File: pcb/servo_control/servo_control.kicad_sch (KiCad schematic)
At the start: 50 parts, among them J1 USB_B_Micro, J10 Conn_01x03_Female, J11 Conn_01x03_Female, J12 Conn_01x03_Female, J13 Conn_01x03_Female, J14 Conn_01x03_Female, J15 Conn_01x03_Female, J16 Conn_01x03_Female, J17 Conn_01x03_Female, J18 Conn_01x03_Female, J19 Conn_01x03_Female, J2 YLIDAR X4, J20 Conn_01x03_Female, J21 Conn_01x06_Male, J3 Conn_01x03_Female, J4 Conn_01x03_Female, J5 Conn_01x03_Female, J6 Conn_01x03_Female, J7 Conn_01x03_Female, J8 Conn_01x03_Female, J9 Conn_01x03_Female, SW1 ESP_PROG, SW2 ESP_RST, U1 PCA9685BS, U2 LM317_SOT-223, U3 ESP32-WROOM-32, U4 MPU-9250, U5 PCA9685BS

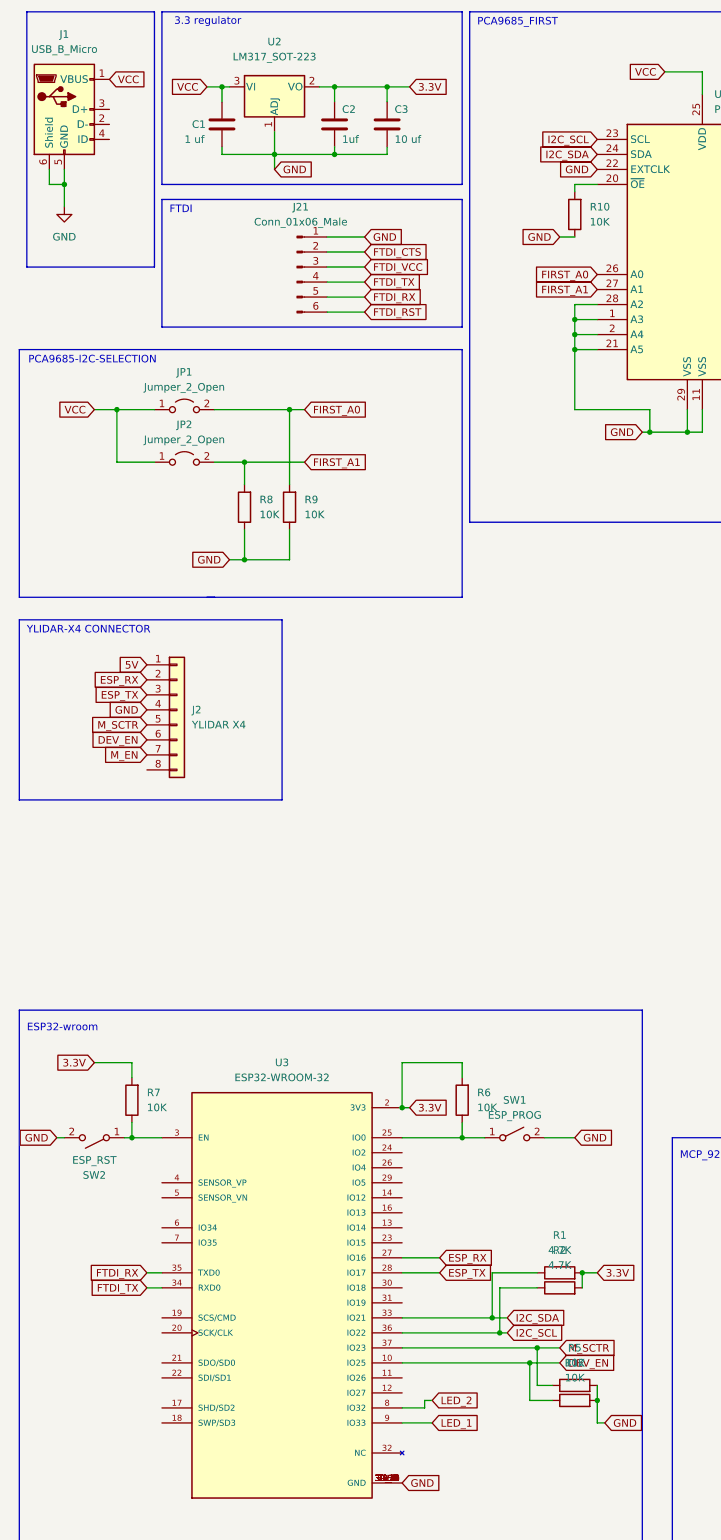
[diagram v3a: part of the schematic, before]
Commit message: add 5V regulator
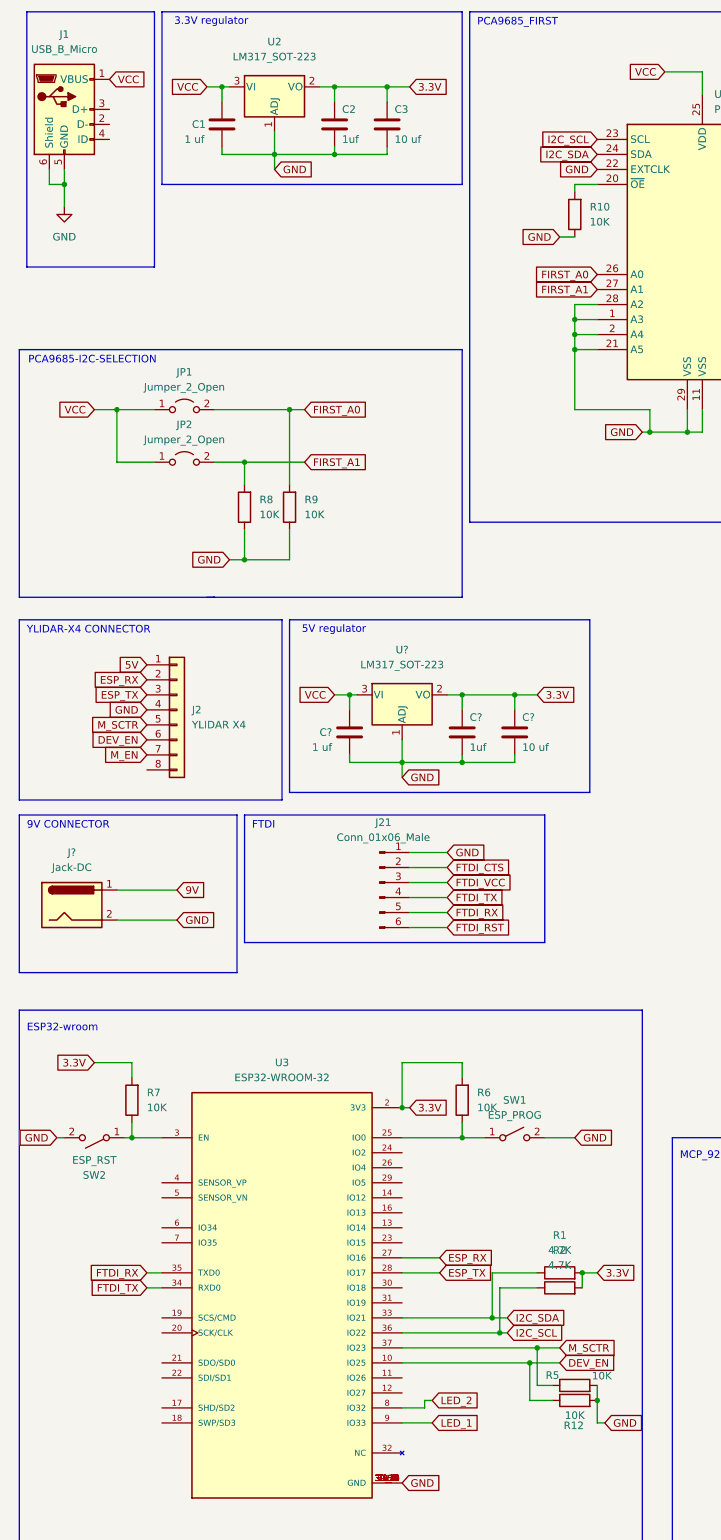
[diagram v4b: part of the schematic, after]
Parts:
- added C?: 1 uf, Capacitor_SMD:C_0603_1608Metric, symbol Device:C
- added C?: 1uf, Capacitor_SMD:C_0603_1608Metric, symbol Device:C
- added C?: 10 uf, Capacitor_SMD:C_0603_1608Metric, symbol Device:C
- added J?: Jack-DC, symbol Connector:Jack-DC
- added U?: LM317_SOT-223, Package_TO_SOT_SMD:SOT-223-3_TabPin2, symbol Regulator_Linear:LM317_SOT-223
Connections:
- net 3.3V: now also C?.1, C?.1, U?.2 (VO)
- net GND: now also C?.2, C?.2, C?.2, J?.2, U?.1 (ADJ)
- net VCC: now also C?.1, U?.3 (VI)
- new net 9V: J?.1
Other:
- note added: "3.3V regulator"
- note added: "5V regulator"
- note added: "9V CONNECTOR"
- note removed: "3.3 regulator"
- moved on the sheet: J21

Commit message: add jack
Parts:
- removed J1: USB_B_Micro, Connector_USB:USB_Micro-B_Molex-105017-0001, symbol Connector:USB_B_Micro
- J1: renamed from J?; footprint (none) -> Connector_BarrelJack:BarrelJack_Horizontal
- gave numbers to parts that had none: 4
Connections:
- net 3.3V: no longer C8.1, C9.1, U6.2 (VO)
- net 5V: now also C8.1, C9.1, U1.25 (VDD), U5.25 (VDD), U6.2 (VO)
- net 9V: now also C1.1, C7.1, U2.3 (VI), U6.3 (VI)
- net VCC: no longer C1.1, C7.1, U1.25 (VDD), U2.3 (VI), U5.25 (VDD), U6.3 (VI)
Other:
- moved on the sheet: D1, D2, R10, R11, R3, R4, U1, U5

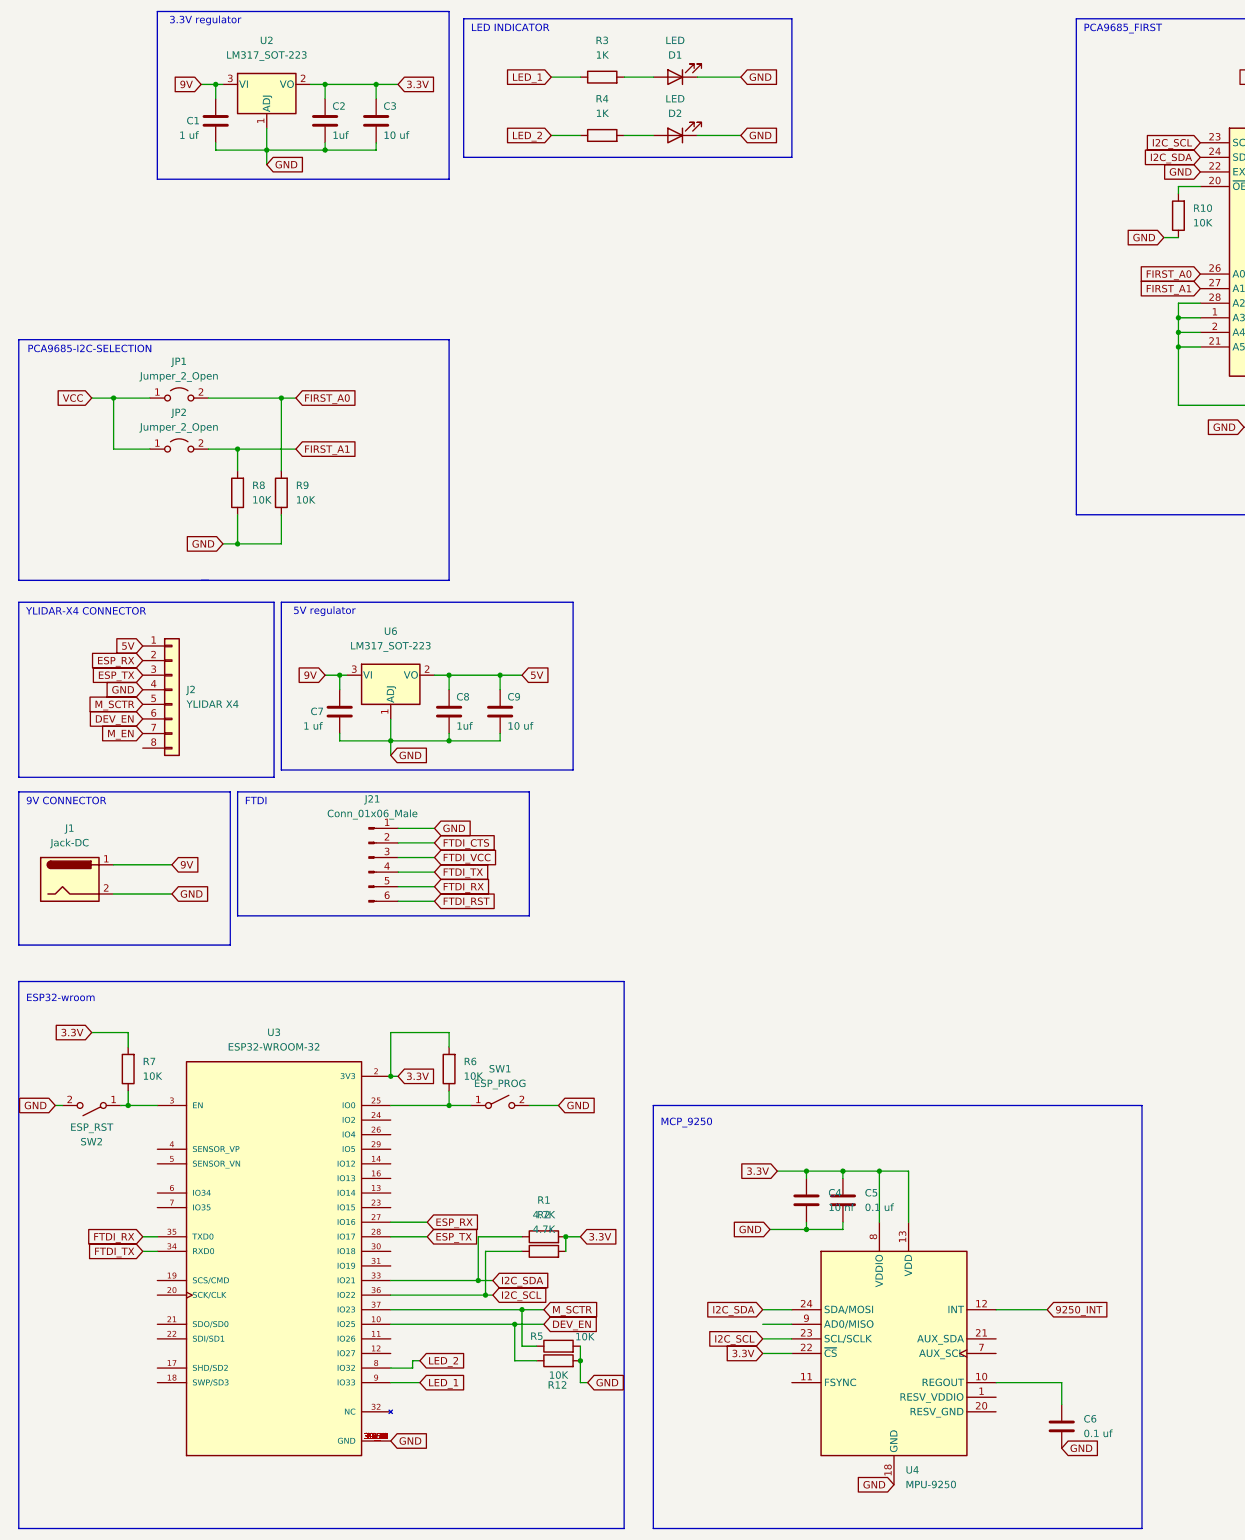
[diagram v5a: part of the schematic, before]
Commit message: add dual cell charger
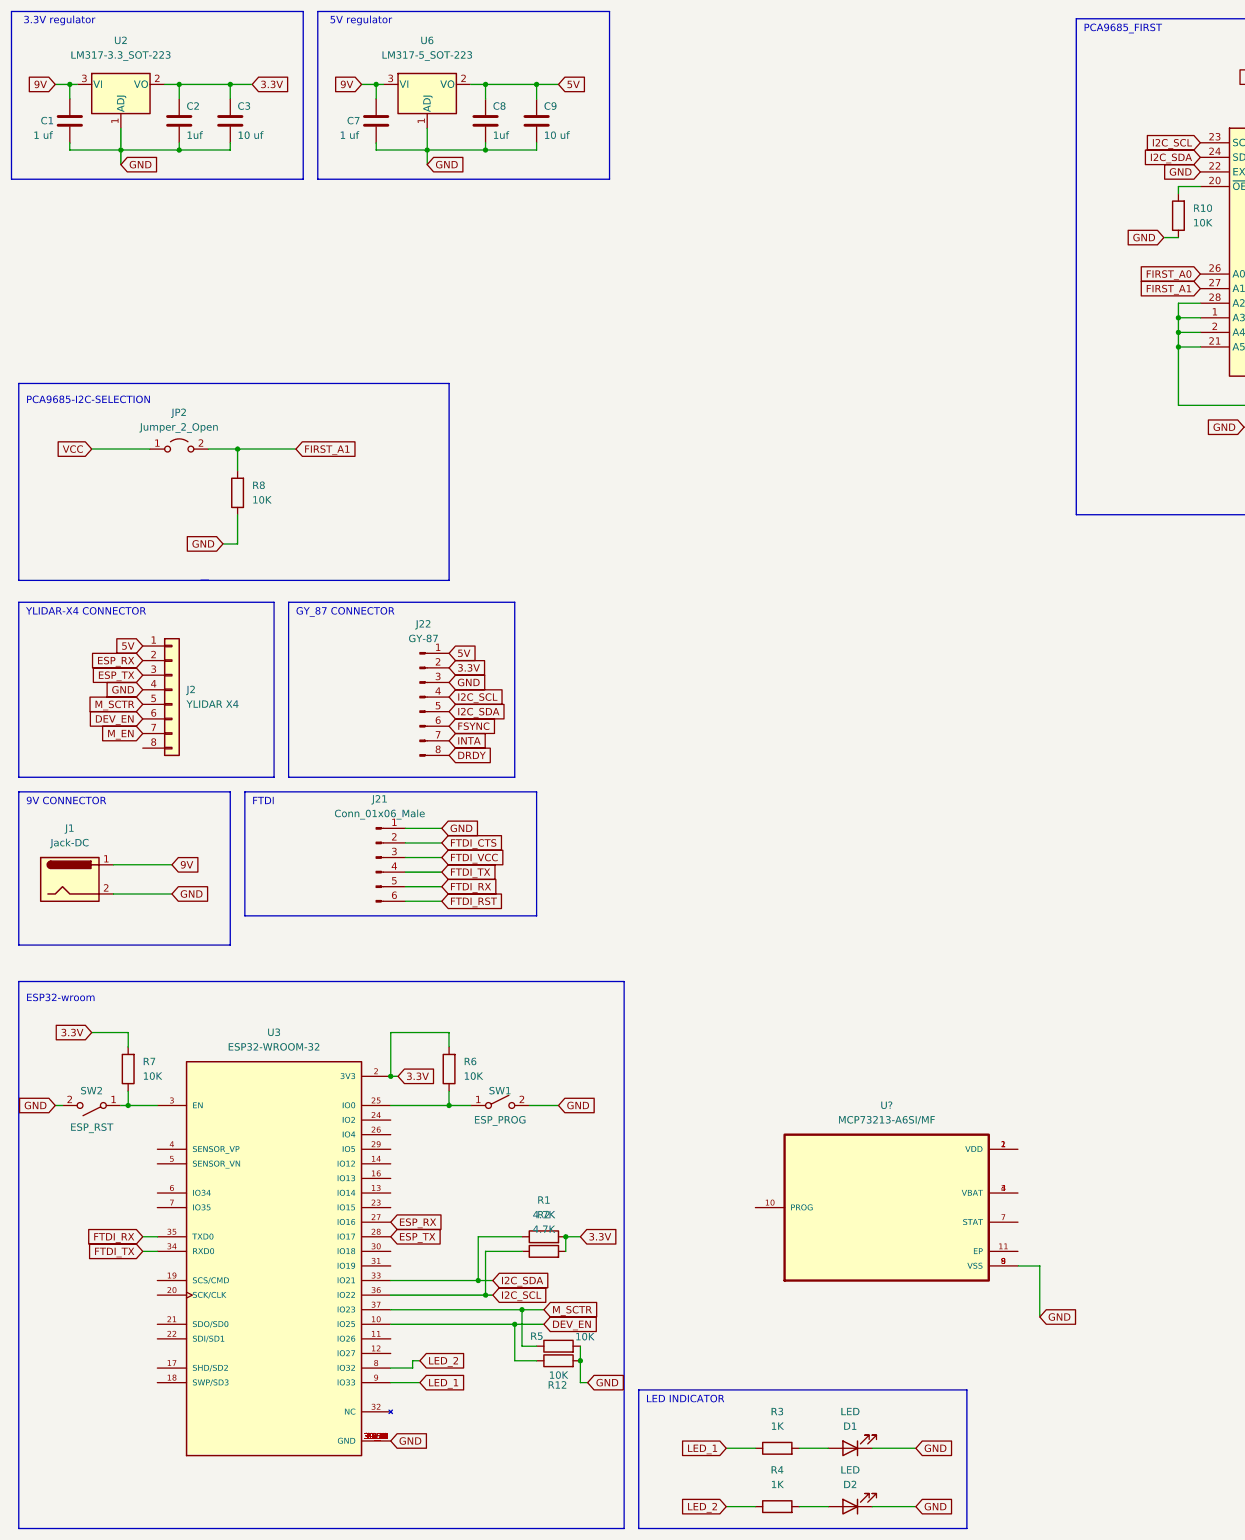
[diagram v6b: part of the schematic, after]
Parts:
- removed C4: 10 nf, Capacitor_SMD:C_0603_1608Metric, symbol Device:C
- removed C5, C6: 0.1 uf, Capacitor_SMD:C_0603_1608Metric, symbol Device:C
- removed JP1: Jumper_2_Open, Jumper:SolderJumper-2_P1.3mm_Bridged2Bar_Pad1.0x1.5mm, symbol Jumper:Jumper_2_Open
- removed R9: 10K, Resistor_SMD:R_0603_1608Metric, symbol Device:R
- removed U4: MPU-9250, Sensor_Motion:InvenSense_QFN-24_3x3mm_P0.4mm, symbol Sensor_Motion:MPU-9250
- added J22: GY-87, Connector_PinHeader_2.54mm:PinHeader_1x08_P2.54mm_Vertical, symbol Connector:Conn_01x08_Male
- added U?: MCP73213-A6SI/MF, MCP73213:SON50P300X300X100-11N, symbol MCP73213:MCP73213-A6SI/MF
- U2: value LM317_SOT-223 -> LM317-3.3_SOT-223
- U6: value LM317_SOT-223 -> LM317-5_SOT-223
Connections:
- net 3.3V: now also J22.2 (Pin_2)
- net 5V: now also J22.1 (Pin_1)
- net GND: now also J22.3 (Pin_3), U?.8 (VSS), U?.9 (VSS)
- net I2C_SCL: now also J22.4 (Pin_4)
- net I2C_SDA: now also J22.5 (Pin_5)
- new net: U?.1 (VDD), U?.2 (VDD)
- new net: U?.3 (VBAT), U?.4 (VBAT)
- new net DRDY: J22.8 (Pin_8)
- new net FSYNC: J22.6 (Pin_6)
- new net INTA: J22.7 (Pin_7)
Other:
- note added: "GY_87 CONNECTOR"
- note removed: "MCP_9250"
- moved on the sheet: C1, C2, C3, C7, C8, C9, D1, D2, J21, R3, R4, U2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

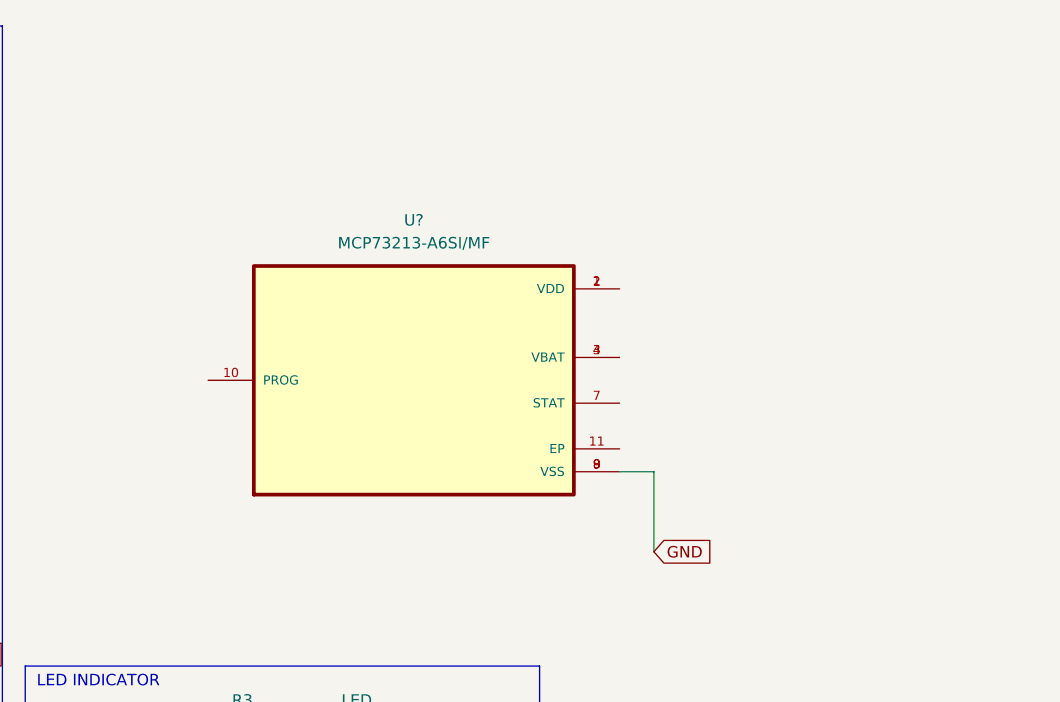
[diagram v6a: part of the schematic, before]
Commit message: add lipo 2S charger
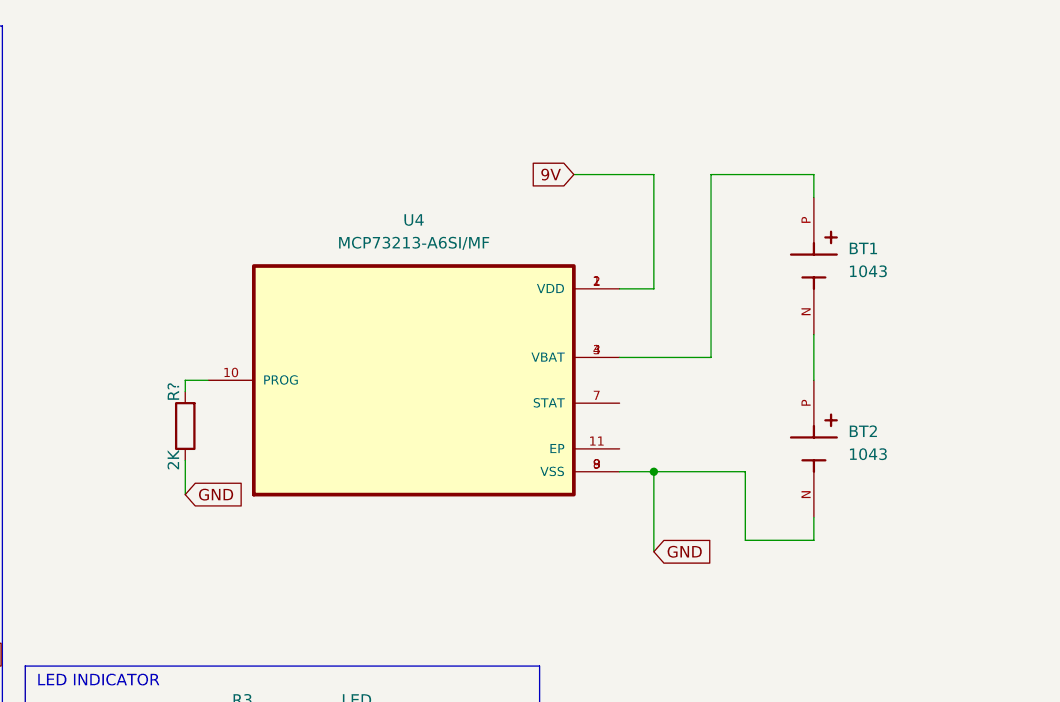
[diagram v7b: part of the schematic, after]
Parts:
- added BT1, BT2: 1043, BAT_1043, symbol 18650:1043
- added R?: 2K, Resistor_SMD:R_0603_1608Metric, symbol Device:R
- gave numbers to parts that had none: 1
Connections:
- net 9V: now also U4.1 (VDD), U4.2 (VDD)
- net GND: now also BT2.N, R?.1
- net at U4.10 (PROG): now also R?.2
- net at U4.3 (VBAT), U4.4 (VBAT): now also BT1.P
- new net: BT1.N, BT2.P
